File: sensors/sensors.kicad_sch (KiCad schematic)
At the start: 9 parts, among them J1 GPIO, J2 JP_CAN, J3 JP_PWM, J4 JP_ADC

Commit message: use solder jumpers
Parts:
- JP1, JP2: footprint Connector_PinHeader_2.54mm:PinHeader_1x03_P2.54mm_Vertical -> Jumper:SolderJumper-3_P1.3mm_Open_RoundedPad1.0x1.5mm
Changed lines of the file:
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@@
 		(in_bom no)
 		(on_board yes)
-		(in_pos_files yes)
+		(in_pos_files no)
 		(dnp no)
 		(fields_autoplaced yes)
@@
 			)
 		)
-		(property "Footprint" "Connector_PinHeader_2.54mm:PinHeader_1x03_P2.54mm_Vertical"
+		(property "Footprint" "Jumper:SolderJumper-3_P1.3mm_Open_RoundedPad1.0x1.5mm"
 			(at 74.93 252.73 0)
 			(hide yes)
@@
 		(in_bom no)
 		(on_board yes)
-		(in_pos_files yes)
+		(in_pos_files no)
 		(dnp no)
 		(fields_autoplaced yes)
@@
 			)
 		)
-		(property "Footprint" "Connector_PinHeader_2.54mm:PinHeader_1x03_P2.54mm_Vertical"
+		(property "Footprint" "Jumper:SolderJumper-3_P1.3mm_Open_RoundedPad1.0x1.5mm"
 			(at 48.26 252.73 0)
 			(hide yes)

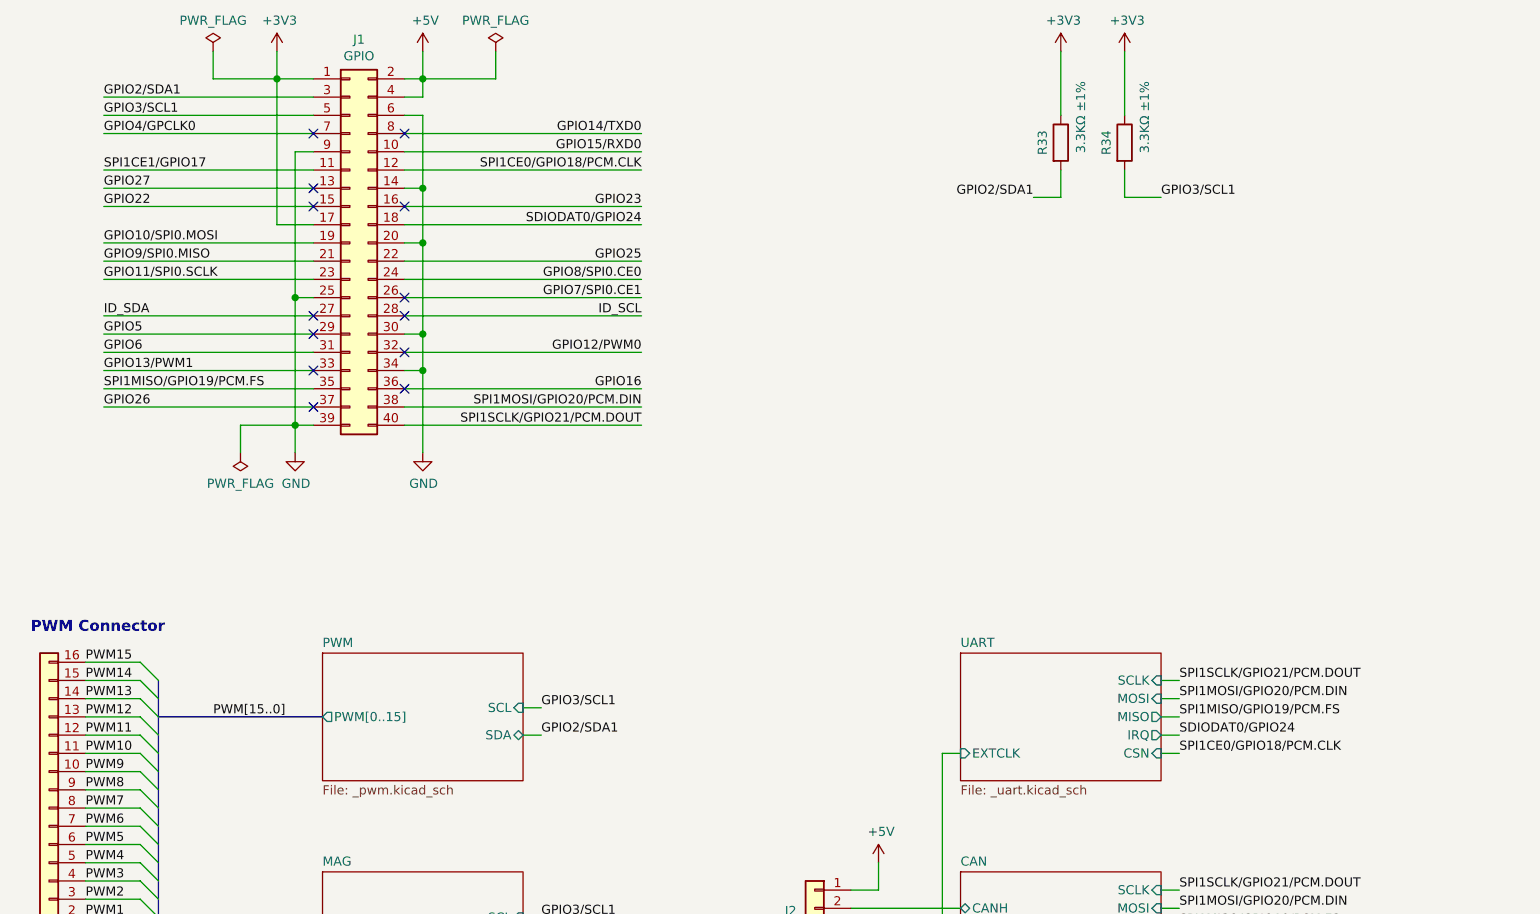
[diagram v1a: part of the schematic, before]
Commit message: changes from dshot branch
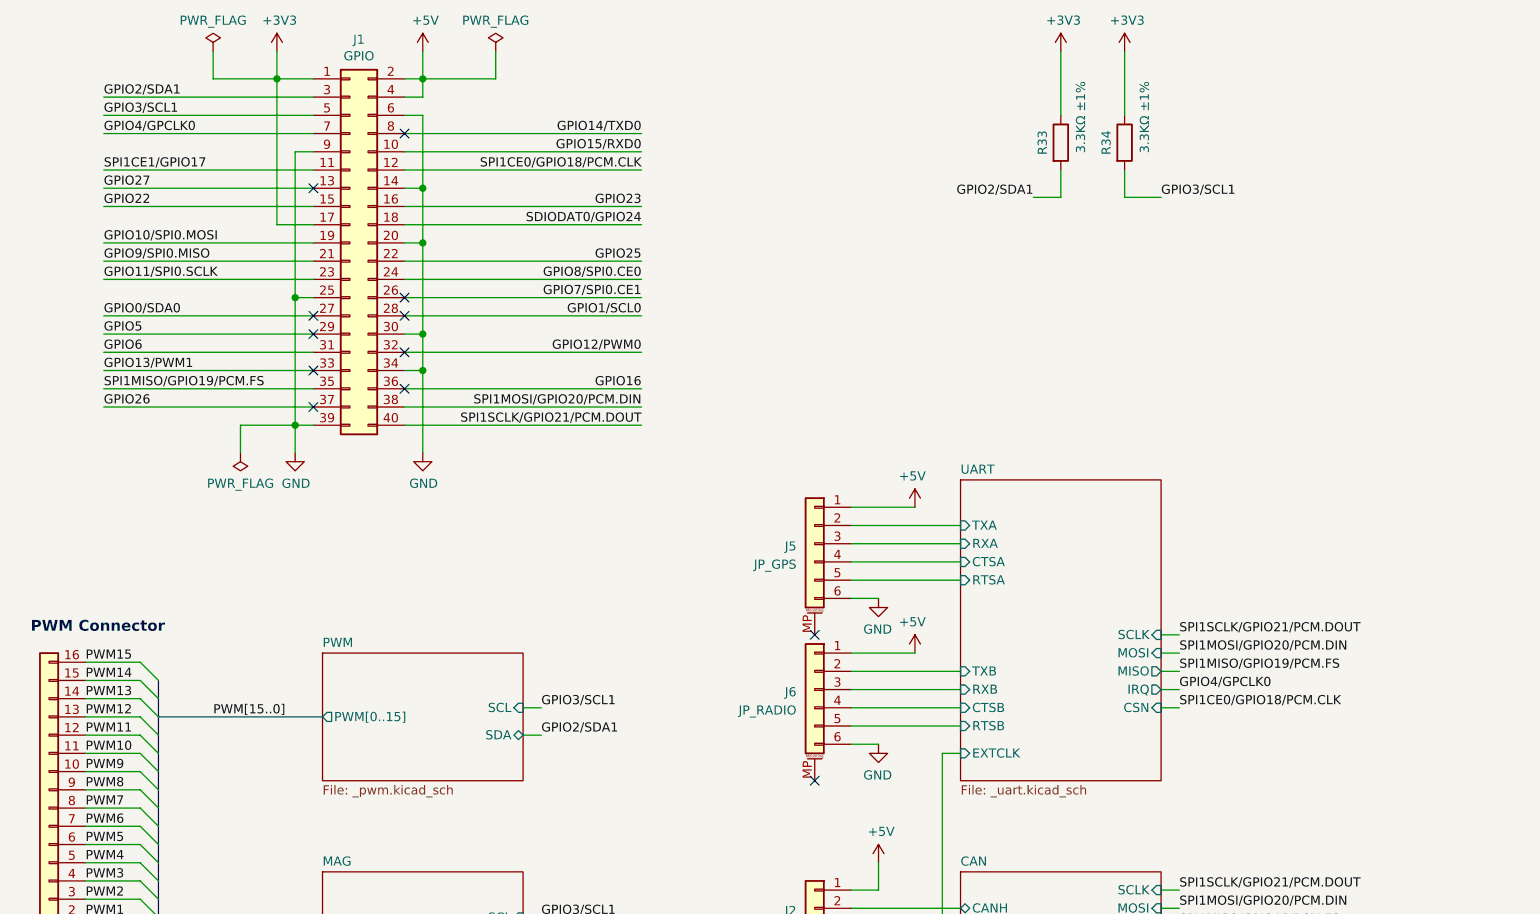
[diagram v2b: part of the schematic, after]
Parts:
- added J5: JP_GPS, Connector_Molex:Molex_PicoBlade_53261-0671_1x06-1MP_P1.25mm_Horizontal, symbol Connector_Generic_MountingPin:Conn_01x06_MountingPin
- added J6: JP_RADIO, Connector_Molex:Molex_PicoBlade_53261-0671_1x06-1MP_P1.25mm_Horizontal, symbol Connector_Generic_MountingPin:Conn_01x06_MountingPin
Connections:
- net +5V: now also J5.1 (Pin_1), J6.1 (Pin_1)
- net GND: now also J5.6 (Pin_6), J6.6 (Pin_6)
- net ID_SCL renamed GPIO1/SCL0
- net ID_SDA renamed GPIO0/SDA0
- new net UART/CTSA: J5.4 (Pin_4)
- new net UART/CTSB: J6.4 (Pin_4)
- new net UART/RTSA: J5.5 (Pin_5)
- new net UART/RTSB: J6.5 (Pin_5)
- new net UART/RXA: J5.3 (Pin_3)
- new net UART/RXB: J6.3 (Pin_3)
- new net UART/TXA: J5.2 (Pin_2)
- new net UART/TXB: J6.2 (Pin_2)
- no-connect marks 14 -> 13
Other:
- sheet UART ports: added CTSA, CTSB, RTSA, RTSB, RXA, RXB, TXA, TXB; removed none

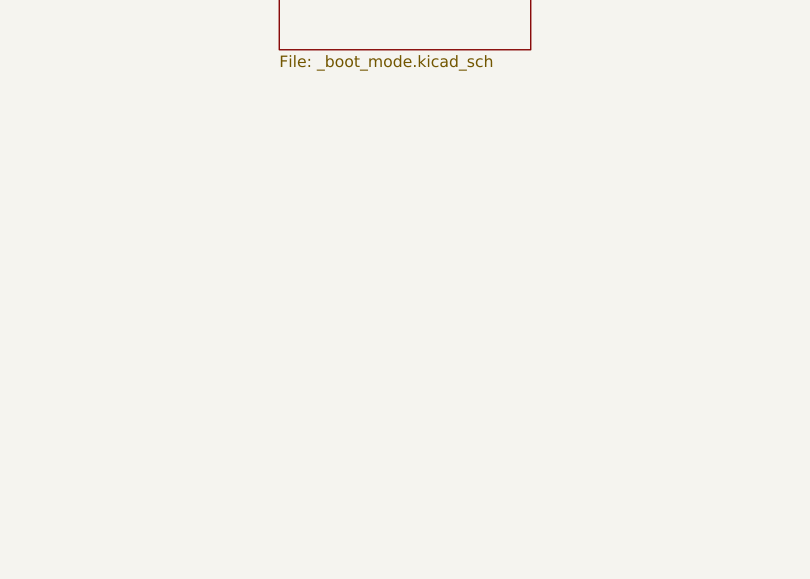
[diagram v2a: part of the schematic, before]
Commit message: added 74ACT595 SIPO for DShot bitbanging
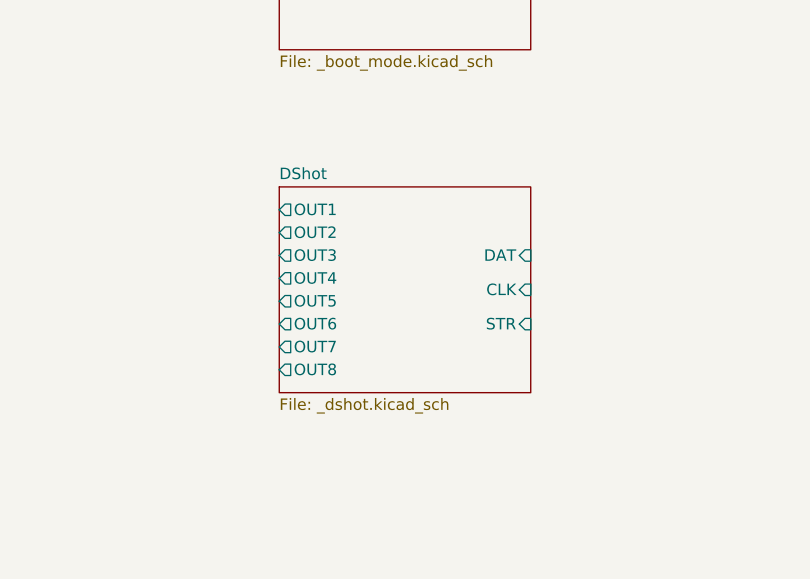
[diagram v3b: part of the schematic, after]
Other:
- added sheet DShot (_dshot.kicad_sch)
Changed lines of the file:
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@@
+	)
+	(sheet
+		(at 266.7 180.34)
+		(size 27.94 22.86)
+		(exclude_from_sim no)
+		(in_bom yes)
+		(on_board yes)
+		(dnp no)
+		(fields_autoplaced yes)
+		(stroke
+			(width 0.1524)
+			(type solid)
+		)
+		(fill
+			(color 0 0 0 0)
+		)
+		(property "Sheetname" "DShot"
+			(at 266.7 179.6284 0)
+			(show_name no)
+			(do_not_autoplace no)
+			(effects
+				(font
+					(size 1.27 1.27)
+				)
+				(justify left bottom)
+			)
+		)
+		(property "Sheetfile" "_dshot.kicad_sch"
+			(at 266.7 203.7846 0)
+			(show_name no)
+			(do_not_autoplace no)
+			(effects
+				(font
+					(size 1.27 1.27)
+				)
+				(justify left top)
+			)
+		)
+		(pin "STR" input
+			(at 294.64 195.58 0)
+			(effects
+				(font
+					(size 1.27 1.27)
+				)
+				(justify right)
+			)
+		)
+		(pin "CLK" input
+			(at 294.64 191.77 0)
+			(effects
+				(font
+					(size 1.27 1.27)
+				)
+				(justify right)
+			)
+		)
+		(pin "DAT" input
+			(at 294.64 187.96 0)
+			(effects
+				(font
+					(size 1.27 1.27)
+				)
+				(justify right)
+			)
+		)
+		(pin "OUT2" output
+			(at 266.7 185.42 180)
+			(effects
+				(font
+					(size 1.27 1.27)
+				)
+				(justify left)
+			)
+		)
+		(pin "OUT3" output
+			(at 266.7 187.96 180)
+			(effects
+				(font
+					(size 1.27 1.27)
+				)
+				(justify left)
+			)
+		)
+		(pin "OUT1" output
+			(at 266.7 182.88 180)
+			(effects
+				(font
+					(size 1.27 1.27)
+				)
+				(justify left)
+			)
+		)
+		(pin "OUT4" output
+			(at 266.7 190.5 180)
+			(effects
+				(font
+					(size 1.27 1.27)
+				)
+				(justify left)
+			)
+		)
+		(pin "OUT5" output
+			(at 266.7 193.04 180)
+			(effects
+				(font
+					(size 1.27 1.27)
+				)
+				(justify left)
+			)
+		)
+		(pin "OUT6" output
+			(at 266.7 195.58 180)
+			(effects
+				(font
+					(size 1.27 1.27)
+				)
+				(justify left)
+			)
+		)
+		(pin "OUT7" output
+			(at 266.7 198.12 180)
+			(effects
+				(font
+					(size 1.27 1.27)
+				)
+				(justify left)
+			)
+		)
+		(pin "OUT8" output
+			(at 266.7 200.66 180)
+			(effects
+				(font
+					(size 1.27 1.27)
+				)
+				(justify left)
+			)
+		)
+		(instances
+			(project "sensors"
+				(path "/e63e39d7-6ac0-4ffd-8aa3-1841a4541b55"
+					(page "11")
+				)
+			)
+		)
 	)
 	(sheet

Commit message: solder pads
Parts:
- removed J6: JP_RADIO, Connector_Molex:Molex_PicoBlade_53261-0671_1x06-1MP_P1.25mm_Horizontal, symbol Connector_Generic_MountingPin:Conn_01x06_MountingPin
- added H1: DSHOT1, Connector_Wire:SolderWirePad_1x01_SMD_1x2mm, symbol Mechanical:MountingHole_Pad
- added H2: DSHOT2, Connector_Wire:SolderWirePad_1x01_SMD_1x2mm, symbol Mechanical:MountingHole_Pad
- added H3: DSHOT3, Connector_Wire:SolderWirePad_1x01_SMD_1x2mm, symbol Mechanical:MountingHole_Pad
- added H4: DSHOT4, Connector_Wire:SolderWirePad_1x01_SMD_1x2mm, symbol Mechanical:MountingHole_Pad
- added H5: DSHOT5, Connector_Wire:SolderWirePad_1x01_SMD_1x2mm, symbol Mechanical:MountingHole_Pad
- added H6: DSHOT6, Connector_Wire:SolderWirePad_1x01_SMD_1x2mm, symbol Mechanical:MountingHole_Pad
- added H7: DSHOT7, Connector_Wire:SolderWirePad_1x01_SMD_1x2mm, symbol Mechanical:MountingHole_Pad
- added H8: DSHOT8, Connector_Wire:SolderWirePad_1x01_SMD_1x2mm, symbol Mechanical:MountingHole_Pad
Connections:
- net +5V: no longer J5.1 (Pin_1)
- net DShot/OUT1: now also H1.1
- net DShot/OUT2: now also H2.1
- net DShot/OUT3: now also H3.1
- net DShot/OUT4: now also H4.1
- net DShot/OUT5: now also H5.1
- net DShot/OUT6: now also H6.1
- net DShot/OUT7: now also H7.1
- net DShot/OUT8: now also H8.1

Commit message: solder pads for dshot; resistor layout
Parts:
- removed H1: DSHOT1, Connector_Wire:SolderWirePad_1x01_SMD_1x2mm, symbol Mechanical:MountingHole_Pad
- removed H2: DSHOT2, Connector_Wire:SolderWirePad_1x01_SMD_1x2mm, symbol Mechanical:MountingHole_Pad
- removed H3: DSHOT3, Connector_Wire:SolderWirePad_1x01_SMD_1x2mm, symbol Mechanical:MountingHole_Pad
- removed H4: DSHOT4, Connector_Wire:SolderWirePad_1x01_SMD_1x2mm, symbol Mechanical:MountingHole_Pad
- removed H5: DSHOT5, Connector_Wire:SolderWirePad_1x01_SMD_1x2mm, symbol Mechanical:MountingHole_Pad
- removed H6: DSHOT6, Connector_Wire:SolderWirePad_1x01_SMD_1x2mm, symbol Mechanical:MountingHole_Pad
- removed H7: DSHOT7, Connector_Wire:SolderWirePad_1x01_SMD_1x2mm, symbol Mechanical:MountingHole_Pad
- removed H8: DSHOT8, Connector_Wire:SolderWirePad_1x01_SMD_1x2mm, symbol Mechanical:MountingHole_Pad
- added J10: DSHOT4, TestPoint:TestPoint_Pad_D1.5mm, symbol Connector_Generic:Conn_01x01
- added J11: DSHOT5, TestPoint:TestPoint_Pad_D1.5mm, symbol Connector_Generic:Conn_01x01
- added J12: DSHOT6, TestPoint:TestPoint_Pad_D1.5mm, symbol Connector_Generic:Conn_01x01
- added J13: DSHOT7, TestPoint:TestPoint_Pad_D1.5mm, symbol Connector_Generic:Conn_01x01
- added J14: DSHOT8, TestPoint:TestPoint_Pad_D1.5mm, symbol Connector_Generic:Conn_01x01
- added J7: DSHOT1, TestPoint:TestPoint_Pad_D1.5mm, symbol Connector_Generic:Conn_01x01
- added J8: DSHOT2, TestPoint:TestPoint_Pad_D1.5mm, symbol Connector_Generic:Conn_01x01
- added J9: DSHOT3, TestPoint:TestPoint_Pad_D1.5mm, symbol Connector_Generic:Conn_01x01
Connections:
- net DShot/OUT1: now also J7.1 (Pin_1)
- net DShot/OUT2: now also J8.1 (Pin_1)
- net DShot/OUT3: now also J9.1 (Pin_1)
- net DShot/OUT4: now also J10.1 (Pin_1)
- net DShot/OUT5: now also J11.1 (Pin_1)
- net DShot/OUT6: now also J12.1 (Pin_1)
- net DShot/OUT7: now also J13.1 (Pin_1)
- net DShot/OUT8: now also J14.1 (Pin_1)

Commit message: lots of changes
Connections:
- no-connect marks 13 -> 11
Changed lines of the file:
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@@
 	)
 	(no_connect
-		(at 130.81 134.62)
-	)
-	(no_connect
 		(at 73.66 67.31)
 	)
 	(no_connect
-		(at 130.81 114.3)
-	)
-	(no_connect
 		(at 73.66 74.93)
 	)
@@
 	(wire
 		(pts
+			(xy 294.64 195.58) (xy 298.45 195.58)
+		)
+		(stroke
+			(width 0)
+			(type default)
+		)
+	)
+	(wire
+		(pts
 			(xy 41.91 212.09) (xy 41.91 214.63)
 		)
@@
 	(wire
 		(pts
+			(xy 294.64 187.96) (xy 298.45 187.96)
+		)
+		(stroke
+			(width 0)
+			(type default)
+		)
+	)
+	(wire
+		(pts
 			(xy 29.21 138.43) (xy 36.83 138.43)
 		)
@@
 	(wire
 		(pts
+			(xy 294.64 191.77) (xy 298.45 191.77)
+		)
+		(stroke
+			(width 0)
+			(type default)
+		)
+	)
+	(wire
+		(pts
 			(xy 139.7 157.48) (xy 139.7 162.56)
 		)
@@
 		)
 	)
+	(label "GPIO22"
+		(at 298.45 187.96 0)
+		(effects
+			(font
+				(size 1.27 1.27)
+			)
+			(justify left bottom)
+		)
+	)
 	(label "PWM5"
 		(at 29.21 143.51 0)
@@
 		)
 	)
+	(label "GPIO23"
+		(at 298.45 191.77 0)
+		(effects
+			(font
+				(size 1.27 1.27)
+			)
+			(justify left bottom)
+		)
+	)
 	(label "GPIO1{slash}SCL0"
 		(at 106.68 69.85 180)
@@
 	)
 	(label "GPIO4{slash}GPCLK0"
-		(at 181.61 121.92 0)
+		(at 181.61 128.27 0)
 		(effects
 			(font
@@
 		)
 	)
+	(label "SDIODAT0{slash}GPIO24"
+		(at 298.45 195.58 0)
+		(effects
+			(font
+				(size 1.27 1.27)
+			)
+			(justify left bottom)
+		)
+	)
 	(symbol
 		(lib_id "power:+5V")
@@
 		)
 		(pin "CLK" input
-			(at 294.64 191.77 0)
+			(at 294.64 187.96 0)
 			(effects
 				(font
@@
 		)
 		(pin "DAT" input
-			(at 294.64 187.96 0)
+			(at 294.64 191.77 0)
 			(effects
 				(font

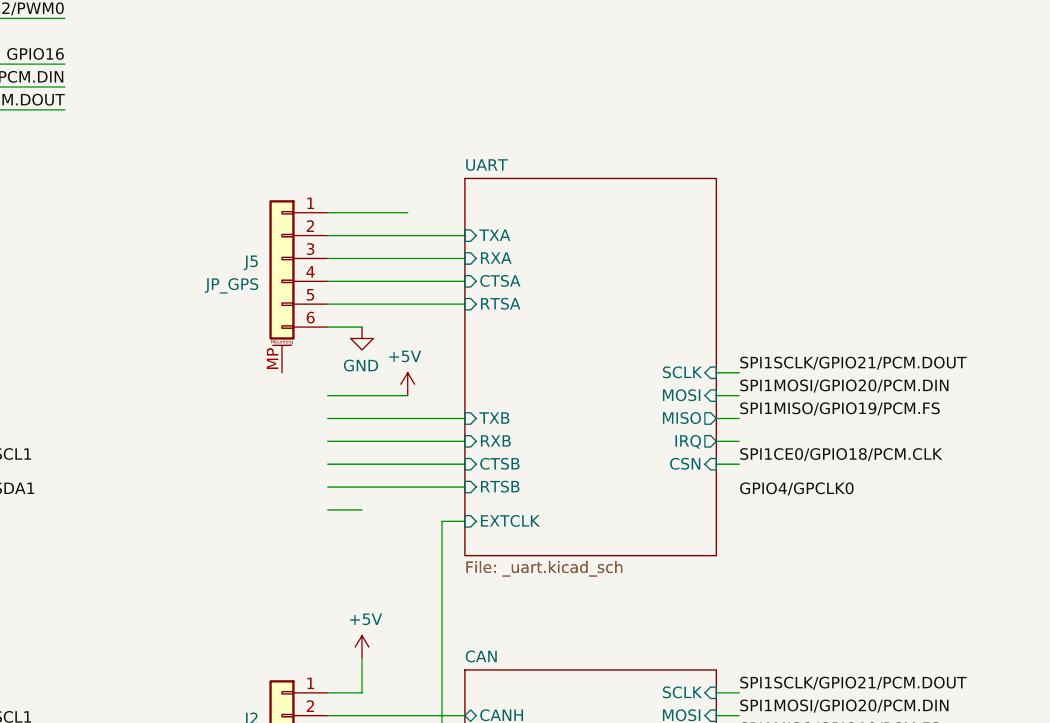
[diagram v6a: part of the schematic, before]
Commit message: use sheet pins for uart connectors
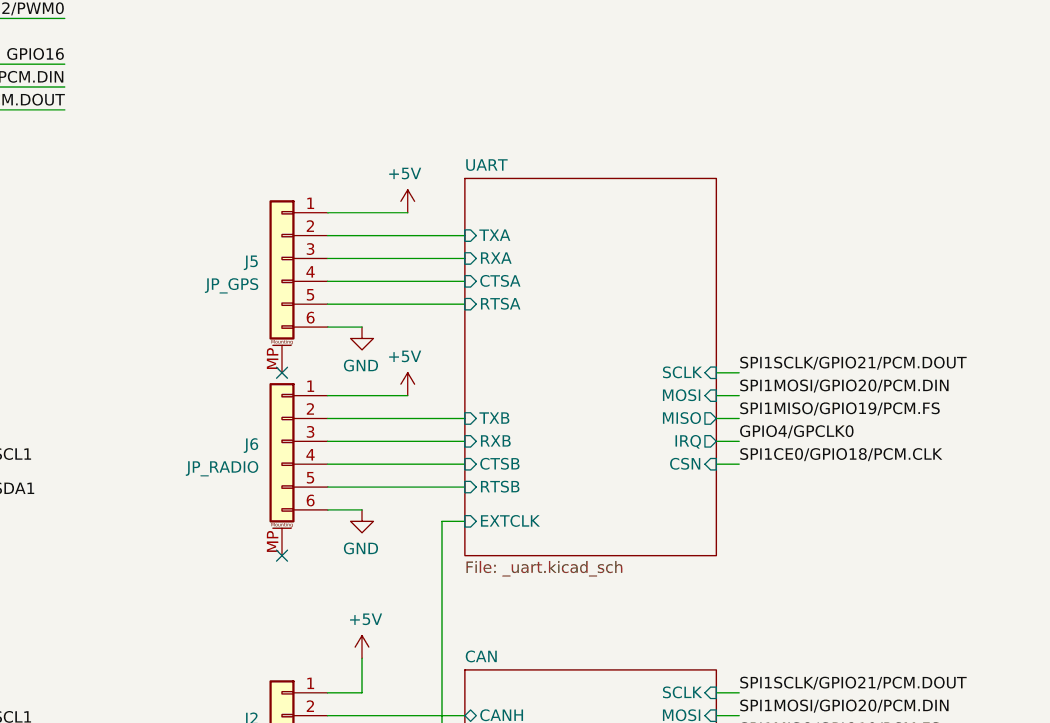
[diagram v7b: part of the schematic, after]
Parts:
- added J6: JP_RADIO, Connector_Molex:Molex_PicoBlade_53261-0671_1x06-1MP_P1.25mm_Horizontal, symbol Connector_Generic_MountingPin:Conn_01x06_MountingPin
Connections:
- net +5V: now also J5.1 (Pin_1), J6.1 (Pin_1)
- net GND: now also J6.6 (Pin_6)
- net UART/CTSB: now also J6.4 (Pin_4)
- net UART/RTSB: now also J6.5 (Pin_5)
- net UART/RXB: now also J6.3 (Pin_3)
- net UART/TXB: now also J6.2 (Pin_2)
- no-connect marks 11 -> 13
